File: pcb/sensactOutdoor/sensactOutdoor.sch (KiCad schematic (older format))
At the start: 104 parts, among them J1 48V, J10 CAN, J11 EXT2, J12 CAN, J2 Conn_01x03, J3 Conn_01x03, J4 PROG, J5 LED CC, J6 PWM_OUT, J7 EXT1, J8 PWM_OUT, J9 230V, K1 ALDP105W, K2 ALDP105W, K3 ALDP105W, K4 ALDP105W, K5 ALDP105W, K6 ALDP105W, Q1 N, Q10 BC847, Q11 BC847, Q2 N, Q3 N, Q4 N, Q5 N, Q6 BC847, Q7 BC847, Q8 BC847, Q9 BC847, U1 ESP32-WROOM-32U, U2 A6211, U3 LMR16006X, U4 SN65HVD230, U5 AMS1117-3.3, U6 RF

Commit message: sensactOutdoor  - pretty schematic & 3D rendering
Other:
- note added: "CAN+1W & RF are\nmutual exclusive"
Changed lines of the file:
@@
 encoding utf-8
 Sheet 1 1
-Title ""
-Date ""
-Rev ""
-Comp ""
+Title "sensactOutdoor"
+Date "2021-03-14"
+Rev "1"
+Comp "Liebler"
 Comment1 ""
 Comment2 ""
@@
 Text Notes 2100 1900 0    50   ~ 0
 Ext. CC Module
+Text Notes 5600 5550 0    50   ~ 0
+CAN+1W & RF are\nmutual exclusive
 $EndSCHEMATC

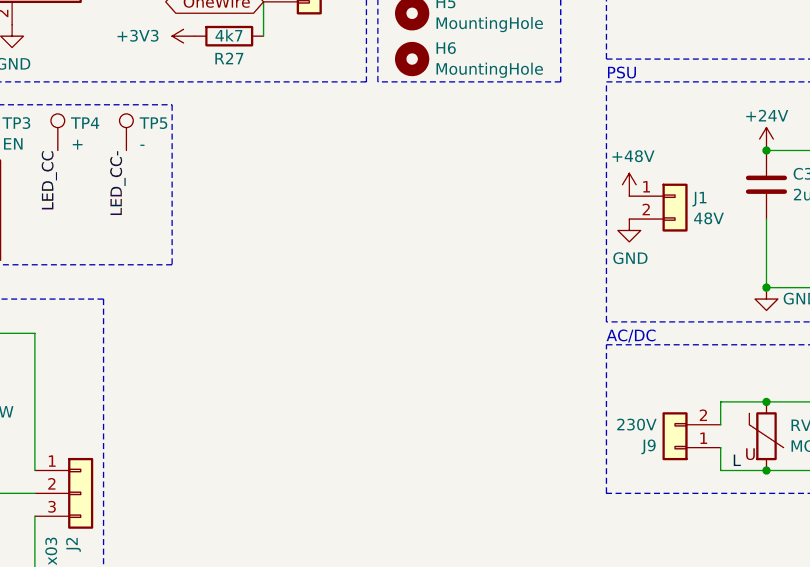
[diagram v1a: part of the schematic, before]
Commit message: Added RX470B 433MHz Module
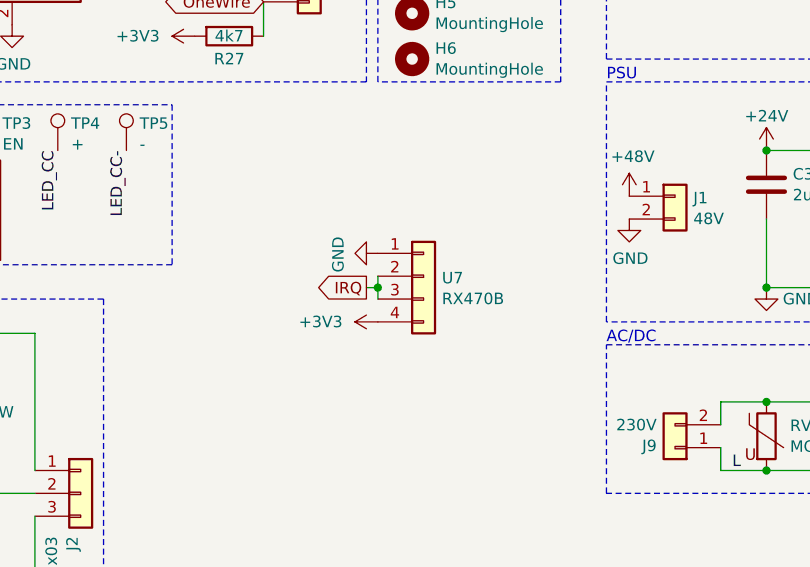
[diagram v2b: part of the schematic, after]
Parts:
- added U7: RX470B, Connector_PinHeader_2.54mm:PinHeader_1x04_P2.54mm_Vertical, symbol Connector_Generic:Conn_01x04
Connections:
- net +3V3: now also U7.4 (Pin_4)
- net GND: now also U7.1 (Pin_1)
- net IRQ: now also U7.2 (Pin_2), U7.3 (Pin_3)
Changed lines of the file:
@@
 Text Notes 5600 5550 0    50   ~ 0
 CAN+1W & RF are\nmutual exclusive
+$Comp
+L Connector_Generic:Conn_01x04 U7
+U 1 1 604E8F64
+P 4800 2650
+F 0 "U7" H 4880 2642 50  0000 L CNN
+F 1 "RX470B" H 4880 2551 50  0000 L CNN
+F 2 "Connector_PinHeader_2.54mm:PinHeader_1x04_P2.54mm_Vertical" H 4800 2650 50  0001 C CNN
+F 3 "~" H 4800 2650 50  0001 C CNN
+	1    4800 2650
+	1    0    0    -1
+$EndComp
+$Comp
+L power:GND #PWR049
+U 1 1 604E9FE8
+P 4600 2550
+F 0 "#PWR049" H 4600 2300 50  0001 C CNN
+F 1 "GND" H 4605 2377 50  0000 C CNN
+F 2 "" H 4600 2550 50  0001 C CNN
+F 3 "" H 4600 2550 50  0001 C CNN
+	1    4600 2550
+	0    1    1    0
+$EndComp
+$Comp
+L power:+3V3 #PWR050
+U 1 1 604EA40E
+P 4600 2850
+F 0 "#PWR050" H 4600 2700 50  0001 C CNN
+F 1 "+3V3" V 4600 3100 50  0000 C CNN
+F 2 "" H 4600 2850 50  0001 C CNN
+F 3 "" H 4600 2850 50  0001 C CNN
+	1    4600 2850
+	0    -1   -1   0
+$EndComp
+Text GLabel 4550 2700 0    50   Output ~ 0
+IRQ
+Wire Wire Line
+	4550 2700 4600 2700
+Wire Wire Line
+	4600 2700 4600 2650
+Wire Wire Line
+	4600 2700 4600 2750
+Connection ~ 4600 2700
 $EndSCHEMATC

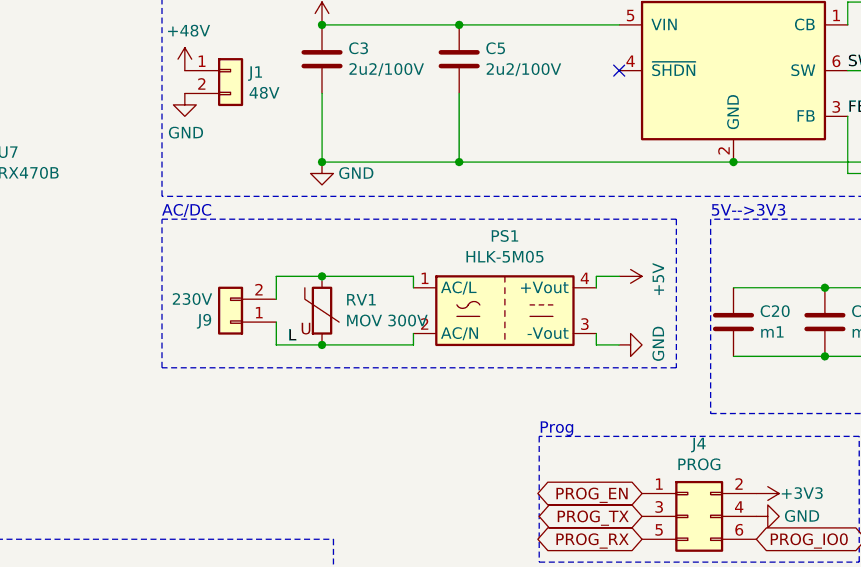
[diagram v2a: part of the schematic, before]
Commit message: added fuse , optimized routing
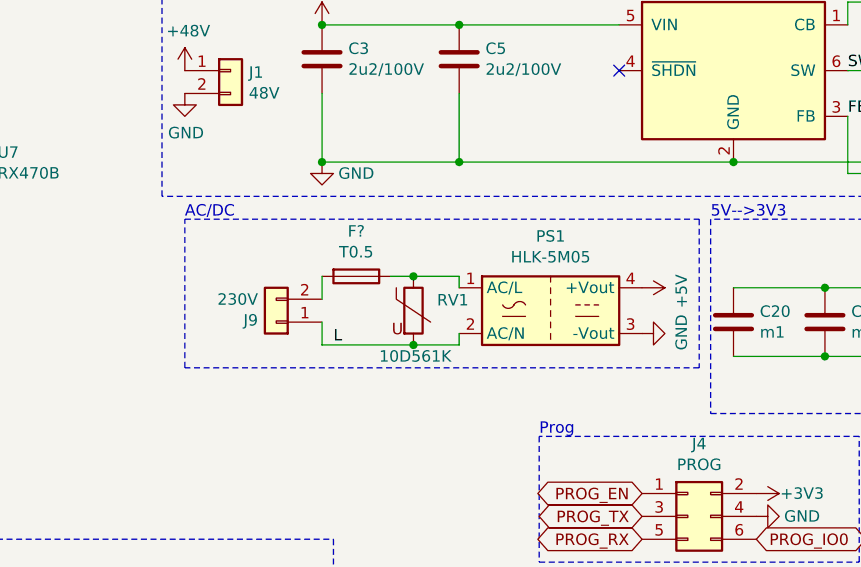
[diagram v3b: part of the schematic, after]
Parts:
- added F?: T0.5, Fuse:Fuse_Littelfuse_372_D8.50mm, symbol Device:Fuse
- RV1: value MOV 300V -> 10D561K; footprint Varistor:RV_Disc_D21.5mm_W5.8mm_P10mm -> Varistor:RV_Disc_D12mm_W6.1mm_P7.5mm
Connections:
- net at PS1.1 (AC/L), RV1.1: now also F?.1; no longer J9.2 (Pin_2)
- new net: F?.2, J9.2 (Pin_2)
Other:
- moved on the sheet: J9, PS1, RV1
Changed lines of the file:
@@
 L Converter_ACDC:HLK-PM01 PS1
 U 1 1 605A8DCF
-P 7100 3350
-F 0 "PS1" H 7100 3675 50  0000 C CNN
-F 1 "HLK-5M05" H 7100 3584 50  0000 C CNN
-F 2 "liebler_MODULES:CONV_HLK-5M05" H 7100 3050 50  0001 C CNN
-F 3 "http://www.hlktech.net/product_detail.php?ProId=54" H 7500 3000 50  0001 C CNN
-	1    7100 3350
+P 7300 3350
+F 0 "PS1" H 7300 3675 50  0000 C CNN
+F 1 "HLK-5M05" H 7300 3584 50  0000 C CNN
+F 2 "liebler_MODULES:CONV_HLK-5M05" H 7300 3050 50  0001 C CNN
+F 3 "http://www.hlktech.net/product_detail.php?ProId=54" H 7700 3000 50  0001 C CNN
+	1    7300 3350
 	1    0    0    -1
 $EndComp
@@
 L Device:Varistor RV1
 U 1 1 605A9FDB
-P 6300 3350
-F 0 "RV1" H 6403 3396 50  0000 L CNN
-F 1 "MOV 300V" H 6403 3305 50  0000 L CNN
-F 2 "Varistor:RV_Disc_D21.5mm_W5.8mm_P10mm" V 6230 3350 50  0001 C CNN
-F 3 "~" H 6300 3350 50  0001 C CNN
-	1    6300 3350
+P 6700 3350
+F 0 "RV1" H 6803 3396 50  0000 L CNN
+F 1 "10D561K" H 6550 3150 50  0000 L CNN
+F 2 "Varistor:RV_Disc_D12mm_W6.1mm_P7.5mm" V 6630 3350 50  0001 C CNN
+F 3 "~" H 6700 3350 50  0001 C CNN
+	1    6700 3350
 	1    0    0    -1
 $EndComp
@@
 L Connector_Generic:Conn_01x02 J9
 U 1 1 605AF4E9
-P 5900 3400
-F 0 "J9" H 5980 3392 50  0000 L CNN
-F 1 "230V" H 5980 3301 50  0000 L CNN
-F 2 "Connector_Phoenix_GMSTB:PhoenixContact_GMSTBVA_2,5_2-G-7,62_1x02_P7.62mm_Vertical" H 5900 3400 50  0001 C CNN
-F 3 "~" H 5900 3400 50  0001 C CNN
-	1    5900 3400
+P 6100 3400
+F 0 "J9" H 6180 3392 50  0000 L CNN
+F 1 "230V" H 6180 3301 50  0000 L CNN
+F 2 "Connector_Phoenix_GMSTB:PhoenixContact_GMSTBVA_2,5_2-G-7,62_1x02_P7.62mm_Vertical" H 6100 3400 50  0001 C CNN
+F 3 "~" H 6100 3400 50  0001 C CNN
+	1    6100 3400
 	-1   0    0    1
 $EndComp
 Wire Wire Line
-	6300 3200 6100 3200
-Wire Wire Line
-	6100 3200 6100 3300
-Wire Wire Line
-	6100 3400 6100 3500
-Wire Wire Line
-	6100 3500 6300 3500
-Wire Wire Line
-	6300 3200 6700 3200
-Wire Wire Line
-	6700 3200 6700 3250
-Connection ~ 6300 3200
+	6300 3200 6300 3300
+Wire Wire Line
+	6300 3400 6300 3500
 Wire Wire Line
 	6300 3500 6700 3500
 Wire Wire Line
-	6700 3500 6700 3450
-Connection ~ 6300 3500
+	6700 3200 6900 3200
+Wire Wire Line
+	6900 3200 6900 3250
+Wire Wire Line
+	6700 3500 6900 3500
+Wire Wire Line
+	6900 3500 6900 3450
+Connection ~ 6700 3500
 $Comp
 L power:+5V #PWR037
 U 1 1 605C7455
-P 7600 3200
-F 0 "#PWR037" H 7600 3050 50  0001 C CNN
-F 1 "+5V" H 7615 3373 50  0000 C CNN
-F 2 "" H 7600 3200 50  0001 C CNN
-F 3 "" H 7600 3200 50  0001 C CNN
-	1    7600 3200
+P 7700 3250
+F 0 "#PWR037" H 7700 3100 50  0001 C CNN
+F 1 "+5V" H 7715 3423 50  0000 C CNN
+F 2 "" H 7700 3250 50  0001 C CNN
+F 3 "" H 7700 3250 50  0001 C CNN
+	1    7700 3250
 	0    1    1    0
 $EndComp
@@
 L power:GND #PWR038
 U 1 1 605C7B08
-P 7600 3500
-F 0 "#PWR038" H 7600 3250 50  0001 C CNN
-F 1 "GND" H 7605 3327 50  0000 C CNN
-F 2 "" H 7600 3500 50  0001 C CNN
-F 3 "" H 7600 3500 50  0001 C CNN
-	1    7600 3500
-	0    -1   -1   0
-$EndComp
-Text Label 6150 3500 0    50   ~ 0
+P 7700 3450
+F 0 "#PWR038" H 7700 3200 50  0001 C CNN
+F 1 "GND" H 7705 3277 50  0000 C CNN
+F 2 "" H 7700 3450 50  0001 C CNN
+F 3 "" H 7700 3450 50  0001 C CNN
+	1    7700 3450
+	0    -1   -1   0
+$EndComp
+Text Label 6350 3500 0    50   ~ 0
 L
 Text Label 2400 3500 0    50   ~ 0
@@
 Text Label 3500 2100 3    50   ~ 0
 LED_CC-
-Wire Wire Line
-	7600 3200 7500 3200
-Wire Wire Line
-	7500 3200 7500 3250
-Wire Wire Line
-	7500 3450 7500 3500
-Wire Wire Line
-	7500 3500 7600 3500
 $Comp
 L RF:NRF24L01_Breakout U6
@@
 I2C Extension
 Wire Notes Line
-	7850 3600 5600 3600
-Wire Notes Line
-	5600 3600 5600 2950
-Wire Notes Line
-	5600 2950 7850 2950
-Wire Notes Line
-	7850 2950 7850 3600
-Text Notes 5600 2950 0    50   ~ 0
+	7950 3600 5700 3600
+Wire Notes Line
+	5700 3600 5700 2950
+Wire Notes Line
+	5700 2950 7950 2950
+Wire Notes Line
+	7950 2950 7950 3600
+Text Notes 5700 2950 0    50   ~ 0
 AC/DC
 Wire Notes Line
@@
 	4600 2700 4600 2750
 Connection ~ 4600 2700
+$Comp
+L Device:Fuse F?
+U 1 1 60502385
+P 6450 3200
+F 0 "F?" V 6253 3200 50  0000 C CNN
+F 1 "T0.5" V 6344 3200 50  0000 C CNN
+F 2 "Fuse:Fuse_Littelfuse_372_D8.50mm" V 6380 3200 50  0001 C CNN
+F 3 "~" H 6450 3200 50  0001 C CNN
+	1    6450 3200
+	0    1    1    0
+$EndComp
+Wire Wire Line
+	6700 3200 6600 3200
+Connection ~ 6700 3200
 $EndSCHEMATC

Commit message: Unsafed Changes (belongs to the previous checkin)
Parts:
- gave numbers to parts that had none: 1
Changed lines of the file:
@@
 Connection ~ 4600 2700
 $Comp
-L Device:Fuse F?
+L Device:Fuse F1
 U 1 1 60502385
 P 6450 3200
-F 0 "F?" V 6253 3200 50  0000 C CNN
+F 0 "F1" V 6253 3200 50  0000 C CNN
 F 1 "T0.5" V 6344 3200 50  0000 C CNN
 F 2 "Fuse:Fuse_Littelfuse_372_D8.50mm" V 6380 3200 50  0001 C CNN

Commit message: Mains Detection
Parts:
- removed D4: SIG_YELLOW, LED_THT:LED_D5.0mm, symbol Device:LED
- added C23: 22n/250V, Capacitor_THT:C_Rect_L11.0mm_W5.1mm_P10.00mm_MKT, symbol Device:C
- added D4: D, Diode_SMD:D_SMA_Handsoldering, symbol Device:D
- added D5: WS2812B, sensact:PLCC4-5050, symbol LED:WS2812B
- added J13: RGB, liebler_CONN:WAGO_250_203, symbol Connector_Generic:Conn_01x03
- added R28: 3k3, Resistor_SMD:R_2512_6332Metric_Pad1.40x3.35mm_HandSolder, symbol Device:R
- added R29: 10k, Resistor_SMD:R_0805_2012Metric_Pad1.20x1.40mm_HandSolder, symbol Device:R
- added R30, R31: 470K, Resistor_SMD:R_2512_6332Metric_Pad1.40x3.35mm_HandSolder, symbol Device:R
- added U8: EL814, liebler_IC:SO-4_7.6x3.6mm_P2.54mm_handsolder, symbol Isolator:EL814
- J10, J12: footprint liebler_CONN:CONN_1-2834011-3 -> liebler_CONN:WAGO_250_203
- R16: value k22 -> 3k3; footprint Resistor_SMD:R_0805_2012Metric_Pad1.20x1.40mm_HandSolder -> Resistor_SMD:R_2512_6332Metric_Pad1.40x3.35mm_HandSolder
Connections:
- net +3V3: now also R29.2
- net +5V: now also D4.2 (A), J13.1 (Pin_1)
- net GND: now also D5.3 (VSS), J13.3 (Pin_3), U8.3; no longer U1.4 (SENSOR_VP)
- net L: now also R28.2
- net SIGNAL: now also D5.4 (DIN); no longer R16.2
- net N: now reaches F1.1, PS1.1 (AC/L), RV1.1
- net N: now also C23.1, R30.2
- net at R16.1: now also U8.1
- new net: D4.1 (K), D5.1 (VDD)
- new net: D5.2 (DOUT), J13.2 (Pin_2)
- new net: C23.2, R31.1, U8.2
- new net: R16.2, R28.1
- new net: R30.1, R31.2
- new net MAINS_AVAILABLE: R29.1, U1.4 (SENSOR_VP), U8.4
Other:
- moved on the sheet: D3, R13

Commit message: sensactOutdoor PCB as ordered at JLCPCB
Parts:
- added C24: 10u, Capacitor_SMD:C_1206_3216Metric_Pad1.33x1.80mm_HandSolder, symbol Device:C
- added J14: N1, liebler_CONN:SolderWirePad_1x01_SMD_2x4mm, symbol Connector_Generic:Conn_01x01
- added J15: N2, liebler_CONN:SolderWirePad_1x01_SMD_2x4mm, symbol Connector_Generic:Conn_01x01
- added R32: k1, Resistor_SMD:R_0805_2012Metric_Pad1.20x1.40mm_HandSolder, symbol Device:R
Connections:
- net GND: now also C24.2
- net N: now also J14.1 (Pin_1); no longer C23.1, R30.2
- net MAINS_AVAILABLE renamed MAINS
- net MAINS: now also C24.1, R32.2; no longer U8.4
- new net: R32.1, U8.4
- new net: C23.1, J15.1 (Pin_1), R30.2
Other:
- moved on the sheet: R29
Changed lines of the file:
@@
 L power:GND #PWR0114
 U 1 1 6051E31D
-P 4950 3750
-F 0 "#PWR0114" H 4950 3500 50  0001 C CNN
-F 1 "GND" H 5100 3700 50  0000 C CNN
-F 2 "" H 4950 3750 50  0001 C CNN
-F 3 "" H 4950 3750 50  0001 C CNN
-	1    4950 3750
+P 5200 3850
+F 0 "#PWR0114" H 5200 3600 50  0001 C CNN
+F 1 "GND" H 5350 3800 50  0000 C CNN
+F 2 "" H 5200 3850 50  0001 C CNN
+F 3 "" H 5200 3850 50  0001 C CNN
+	1    5200 3850
 	1    0    0    -1
 $EndComp
-Text GLabel 5000 3550 2    50   Output ~ 0
-MAINS_AVAILABLE
+Text GLabel 5300 3550 2    50   Output ~ 0
+MAINS
 $Comp
 L Device:R R29
 U 1 1 6051FA1B
-P 4950 3400
-F 0 "R29" V 5050 3400 50  0000 C CNN
-F 1 "10k" V 4950 3400 50  0000 C CNN
-F 2 "Resistor_SMD:R_0805_2012Metric_Pad1.20x1.40mm_HandSolder" V 4880 3400 50  0001 C CNN
-F 3 "~" H 4950 3400 50  0001 C CNN
-	1    4950 3400
+P 5200 3400
+F 0 "R29" V 5300 3400 50  0000 C CNN
+F 1 "10k" V 5200 3400 50  0000 C CNN
+F 2 "Resistor_SMD:R_0805_2012Metric_Pad1.20x1.40mm_HandSolder" V 5130 3400 50  0001 C CNN
+F 3 "~" H 5200 3400 50  0001 C CNN
+	1    5200 3400
 	-1   0    0    1
 $EndComp
-Wire Wire Line
-	5000 3550 4950 3550
 $Comp
 L power:+3V3 #PWR0115
 U 1 1 605299DB
-P 4950 3250
-F 0 "#PWR0115" H 4950 3100 50  0001 C CNN
-F 1 "+3V3" H 4965 3423 50  0000 C CNN
-F 2 "" H 4950 3250 50  0001 C CNN
-F 3 "" H 4950 3250 50  0001 C CNN
-	1    4950 3250
+P 5200 3250
+F 0 "#PWR0115" H 5200 3100 50  0001 C CNN
+F 1 "+3V3" H 5215 3423 50  0000 C CNN
+F 2 "" H 5200 3250 50  0001 C CNN
+F 3 "" H 5200 3250 50  0001 C CNN
+	1    5200 3250
 	1    0    0    -1
 $EndComp
@@
 Text Label 6800 3200 0    50   ~ 0
 N
-Text Label 3750 3750 0    50   ~ 0
+Text Label 3600 3150 0    50   ~ 0
 N
 Text Label 3750 3500 0    50   ~ 0
 L
 Text GLabel 3950 5250 0    50   Input ~ 0
-MAINS_AVAILABLE
+MAINS
 $Comp
 L Isolator:EL814 U8
@@
 	1    0    0    -1
 $EndComp
-Connection ~ 4950 3550
 $Comp
 L Device:R R28
@@
 	4350 3900 4200 3900
 Connection ~ 4350 3750
+Wire Wire Line
+	3750 3900 3600 3900
+Connection ~ 3750 3900
+$Comp
+L Connector_Generic:Conn_01x01 J14
+U 1 1 60536FB7
+P 3600 3350
+F 0 "J14" V 3472 3430 50  0000 L CNN
+F 1 "N1" V 3563 3430 50  0000 L CNN
+F 2 "liebler_CONN:SolderWirePad_1x01_SMD_2x4mm" H 3600 3350 50  0001 C CNN
+F 3 "~" H 3600 3350 50  0001 C CNN
+	1    3600 3350
+	0    1    1    0
+$EndComp
+$Comp
+L Connector_Generic:Conn_01x01 J15
+U 1 1 605433F7
+P 3600 3700
+F 0 "J15" V 3564 3612 50  0000 R CNN
+F 1 "N2" V 3473 3612 50  0000 R CNN
+F 2 "liebler_CONN:SolderWirePad_1x01_SMD_2x4mm" H 3600 3700 50  0001 C CNN
+F 3 "~" H 3600 3700 50  0001 C CNN
+	1    3600 3700
+	0    -1   -1   0
+$EndComp
+$Comp
+L Device:R R32
+U 1 1 6052AA7B
+P 4950 3400
+F 0 "R32" V 5050 3400 50  0000 C CNN
+F 1 "k1" V 4950 3400 50  0000 C CNN
+F 2 "Resistor_SMD:R_0805_2012Metric_Pad1.20x1.40mm_HandSolder" V 4880 3400 50  0001 C CNN
+F 3 "~" H 4950 3400 50  0001 C CNN
+	1    4950 3400
+	-1   0    0    1
+$EndComp
+$Comp
+L Device:C C24
+U 1 1 6052B3D9
+P 5200 3700
+F 0 "C24" H 5315 3746 50  0000 L CNN
+F 1 "10u" H 5315 3655 50  0000 L CNN
+F 2 "Capacitor_SMD:C_1206_3216Metric_Pad1.33x1.80mm_HandSolder" H 5238 3550 50  0001 C CNN
+F 3 "~" H 5200 3700 50  0001 C CNN
+	1    5200 3700
+	1    0    0    -1
+$EndComp
+Connection ~ 5200 3550
+Wire Wire Line
+	5200 3550 5300 3550
+Wire Wire Line
+	4950 3750 4950 3850
+Wire Wire Line
+	4950 3850 5200 3850
+Connection ~ 5200 3850
+Wire Wire Line
+	4950 3250 5050 3250
+Wire Wire Line
+	5050 3250 5050 3550
+Wire Wire Line
+	5050 3550 5200 3550
 $EndSCHEMATC

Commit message: variousChanges on sensactHSIO3+4 and sensactOutdoor
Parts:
- added D6: NUP2105L, Package_TO_SOT_SMD:SOT-23_Handsoldering, symbol Power_Protection:NUP2105L
- added R33: 120R, Resistor_SMD:R_1206_3216Metric_Pad1.30x1.75mm_HandSolder, symbol Device:R
- added SW1: TERM ON OFF, liebler_MECH:SW_SPDT_PCM12_handsolder, symbol Switch:SW_SPDT
- J10, J12, J13: footprint liebler_CONN:WAGO_250_203 -> liebler_CONN:KF250-3.5-3P-A
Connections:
- net CANH: now also J10.1 (Pin_1), J12.3 (Pin_3), D6.2 (K), R33.1; no longer J10.3 (Pin_3), J12.1 (Pin_1)
- net CANL: now also J10.3 (Pin_3), D6.1 (K), SW1.2 (B); no longer J10.1 (Pin_1)
- net GND: now also D6.3 (A)
- net OneWire: now also J12.1 (Pin_1); no longer J12.3 (Pin_3)
- new net: R33.2, SW1.1 (A)
- no-connect marks 8 -> 9
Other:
- moved on the sheet: H1, H2, H3, H4, H5, H6, J10, J12, R27, U7
